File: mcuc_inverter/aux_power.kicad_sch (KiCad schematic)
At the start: 0 parts

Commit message: Capture aux_power sheet: full D020 rail tree, 7 blocks
INN3990CQ flyback per datasheet Fig. 10 / DER-948Q (series-string
input films, RCD clamp, custom 3-winding transformer symbol with
Lp/VOR/isolation notes, bias->BPP, Schottky secondary, FB 143k/13.2k
-> 14.97 V, SR and IS tied to GND per datasheet for diode operation);
LM5175 buck-boost aux path (15.02 V, deliberately above the
diode-dropped flyback so aux carries the load when present) through
LM74610-Q1 + external FET; two LMR51430 bucks (5 V: 71.5k/9.76k;
12 V: 115k/6.04k); TLV1117-33 3.3 V (PWR_FLAG moved here from the
MCU sheet - this is the rail's true source); 4x SN6505B + WE
750316856 gate supplies (winding CT pinout verified from the WE
drawing; +17.9/-5.1 zener splits); NXE2S0505MC isolated CAN 5 V.

All 12 VGD nets verified in the netlist to span aux_power sources
and gate_drive loads (e.g. VGD_HS1_P = rectifiers + caps + U301
VCC2), independently re-checked before commit. ERC 0 errors.

Co-Authored-By: Claude Fable 5 <noreply@anthropic.com>
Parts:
- added C601, C602: 0.68uF 630V film [TBV], Capacitor_SMD:C_0603_1608Metric, symbol Device:C
- added C603: 10nF 1kV [TBV], Capacitor_SMD:C_0603_1608Metric, symbol Device:C
- added C604: 10uF 50V [TBV], Capacitor_SMD:C_0603_1608Metric, symbol Device:C
- added C606: 4.7uF 25V X7R [TBV], Capacitor_SMD:C_0603_1608Metric, symbol Device:C
- added C607: 100nF [TBV], Capacitor_SMD:C_0603_1608Metric, symbol Device:C
- added C608: 1nF 100V [TBV], Capacitor_SMD:C_0603_1608Metric, symbol Device:C
- added C609, C610: 220uF 25V polymer [TBV], symbol Device:C_Polarized
- added C611, C622, C623, C642, C646, C661, C663, C665, C667, C669, C671, C673, C675, C677, C679, C681, C683: 100nF, Capacitor_SMD:C_0603_1608Metric, symbol Device:C
- added C612: 330pF [TBV], Capacitor_SMD:C_0603_1608Metric, symbol Device:C
- added C613, C625: 10nF [TBV], Capacitor_SMD:C_0603_1608Metric, symbol Device:C
- added C614: 2.2uF 25V X7R, Capacitor_SMD:C_0603_1608Metric, symbol Device:C
- added C620, C621: 4.7uF 50V [TBV], Capacitor_SMD:C_0805_2012Metric, symbol Device:C
- added C624: 4.7uF [TBV], Capacitor_SMD:C_0603_1608Metric, symbol Device:C
- added C626, C628: 100pF [TBV], Capacitor_SMD:C_0603_1608Metric, symbol Device:C
- added C627: 47nF [TBV], Capacitor_SMD:C_0603_1608Metric, symbol Device:C
- added C629, C630, C643, C644, C647, C648: 22uF 25V [TBV], Capacitor_SMD:C_1210_3225Metric, symbol Device:C
- added C631: 1uF [TBV], Capacitor_SMD:C_0603_1608Metric, symbol Device:C
- added C640, C645: 2.2uF 50V [TBV], Capacitor_SMD:C_0805_2012Metric, symbol Device:C
- added C650, C651, C653, C660, C666, C672, C678: 10uF [TBV], Capacitor_SMD:C_0805_2012Metric, symbol Device:C
- added C652: 2.2uF [TBV], Capacitor_SMD:C_0603_1608Metric, symbol Device:C
- added C662, C664, C668, C670, C674, C676, C680, C682: 10uF 25V [TBV], Capacitor_SMD:C_0805_2012Metric, symbol Device:C
- added D601: US1M-class 1kV std recovery [TBV], Diode_SMD:D_SOD-323, symbol Device:D
- added D602: BAS316-class [TBV], Diode_SMD:D_SOD-323, symbol Device:D
- added D603: SS310-class 100V 3A [TBV], Diode_SMD:D_SMA, symbol Device:D_Schottky
- added D604: SS54 [TBV], Diode_SMD:D_SMA, symbol Device:D_Schottky
- added D605, D606, D608, D609, D611, D612, D614, D615: SS310 [TBV], Diode_SMD:D_SMA, symbol Device:D_Schottky
- added D607, D610, D613, D616: BZX384-C5V1 [TBV], Diode_SMD:D_SOD-323, symbol Device:D_Zener
- added L601: 10uH [TBV], symbol Device:L
- added L602: 4.7uH [TBV], symbol Device:L
- added L603: 12uH [TBV], symbol Device:L
- added Q601, Q602, Q603, Q604, Q605: CSD18543Q3A-class [TBV], symbol Transistor_FET:CSD18543Q3A
- added R603, R604: 390k 0.5W [TBV], Resistor_SMD:R_0603_1608Metric, symbol Device:R
- added R605: 4.7R 0.5W [TBV], Resistor_SMD:R_0603_1608Metric, symbol Device:R
- added R606: 8.2k [TBV], Resistor_SMD:R_0603_1608Metric, symbol Device:R
- added R607: 100R [TBV], Resistor_SMD:R_0603_1608Metric, symbol Device:R
- added R608: 10R [TBV], Resistor_SMD:R_0603_1608Metric, symbol Device:R
- added R609: 143k 1%, Resistor_SMD:R_0603_1608Metric, symbol Device:R
- added R610: 13.2k 1%, Resistor_SMD:R_0603_1608Metric, symbol Device:R
- added R611: 10k [TBV], Resistor_SMD:R_0603_1608Metric, symbol Device:R
- added R620: 100k [TBV], Resistor_SMD:R_0603_1608Metric, symbol Device:R
- added R621: 16.2k [TBV], Resistor_SMD:R_0603_1608Metric, symbol Device:R
- added R622: 10mR 1% [TBV], Resistor_SMD:R_2512_6332Metric, symbol Device:R
- added R623: 88.7k 1%, Resistor_SMD:R_0603_1608Metric, symbol Device:R
- added R624: 4.99k 1%, Resistor_SMD:R_0603_1608Metric, symbol Device:R
- added R625: 24.9k [TBV], Resistor_SMD:R_0603_1608Metric, symbol Device:R
- added R626: 84.5k (300kHz) [TBV], Resistor_SMD:R_0603_1608Metric, symbol Device:R
- added R627: 93.1k (CCM+hiccup) [TBV], Resistor_SMD:R_0603_1608Metric, symbol Device:R
- added R640: 71.5k 1%, Resistor_SMD:R_0603_1608Metric, symbol Device:R
- added R641: 9.76k 1%, Resistor_SMD:R_0603_1608Metric, symbol Device:R
- added R642: 115k 1%, Resistor_SMD:R_0603_1608Metric, symbol Device:R
- added R643: 6.04k 1%, Resistor_SMD:R_0603_1608Metric, symbol Device:R
- added T601: custom flyback, Lp<500uH, VOR raised for 15 V out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, symbol mcuc:T_FLYBACK_AUX
- added T602, T603, T604, T605: 750316856, symbol mcuc:WE750316856
- added U601: INN3990CQ, symbol mcuc:INN3990CQ
- added U603: LM5175RHFR, symbol Regulator_Switching:LM5175RHF
- added U604: LM74610QDGKRQ1, symbol mcuc:LM74610-Q1
- added U605, U606: LMR51430XDDCR, symbol Regulator_Switching:LMR51430
- added U607: TLV1117-33, Package_TO_SOT_SMD:SOT-223-3_TabPin2, symbol Regulator_Linear:TLV1117-33
- added U608: NXE2S0505MC, symbol mcuc:NXE2S0505MC
- added U609, U610, U611, U612: SN6505BDBVR, symbol Power_Management:SN6505BDBV
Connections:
- new net: C642.2, L602.1, U605.2 (SW)
- new net: C642.1, U605.6 (CB)
- new net: D601.1 (K), R605.2
- new net: D601.2 (A), T601.2 (PRI-), U601.24 (D)
- new net: C612.1, C613.2, R609.2, R610.1, U601.3 (FB)
- new net: C603.2, R603.2, R604.2, R605.1
- new net: Q603.1 (G), U603.18 (LDRV2)
- new net: C614.1, U601.4 (BPS)
- new net: Q601.1 (G), U603.24 (HDRV1)
- new net: C613.1, R611.2
- new net: C606.1, C607.1, R606.2, U601.14 (BPP)
- new net: R607.2, U601.7 (FWD)
- new net: D606.2 (A), T602.4 (N4.B)
- new net: Q604.1 (G), U603.16 (HDRV2)
- new net: C623.1, U603.17 (BOOT2)
- new net: Q602.1 (G), U603.22 (LDRV1)
- new net: C622.1, U603.23 (BOOT1)
- new net: R620.2, R621.1, U603.26 (EN/UVLO)
- new net: D609.2 (A), T603.4 (N4.B)
- new net: D614.2 (A), T605.6 (N3.A)
- new net: D612.2 (A), T604.4 (N4.B)
- new net: D603.2 (A), R607.1, R608.1, T601.5 (SEC+)
- new net: C608.1, R608.2
- new net: C631.1, U604.7 (VCAPH)
- new net: C631.2, U604.1 (VCAPL)
- new net: D605.2 (A), T602.6 (N3.A)
- new net: C625.1, R625.2
- new net: T605.1 (N1.A), U612.1 (D1)
- new net: T605.3 (N2.B), U612.3 (D2)
- new net: C646.1, U606.6 (CB)
- new net: C646.2, L603.1, U606.2 (SW)
- new net: D615.2 (A), T605.4 (N4.B)
- new net: C601.2, C602.1
- new net: T603.1 (N1.A), U610.1 (D1)
- new net: T603.3 (N2.B), U610.3 (D2)
- new net: T602.1 (N1.A), U609.1 (D1)
- new net: T602.3 (N2.B), U609.3 (D2)
- new net: Q605.1 (G), U604.2 (GATE_PD), U604.6 (GATE_DRV)
- new net: C604.1, D602.1 (K), R606.1
- new net: D611.2 (A), T604.6 (N3.A)
- new net: D608.2 (A), T603.6 (N3.A)
- new net: D602.2 (A), T601.3 (BIAS+)
- new net: T604.1 (N1.A), U611.1 (D1)
- new net: T604.3 (N2.B), U611.3 (D2)
- new net +12V: C647.1, C648.1, L603.2, R642.1
- new net +3.3V: C651.1, U607.2 (VO)
- new net +5V: C643.1, C644.1, C650.1, C652.1, C660.1, C661.1, C666.1, C667.1, C672.1, C673.1, C678.1, C679.1, L602.2, R640.1, T602.2 (CT_PRI), T603.2 (CT_PRI), T604.2 (CT_PRI), T605.2 (CT_PRI), U607.3 (VI), U608.3 (+VIN), U609.2 (VCC), U609.5 (EN), U610.2 (VCC), U610.5 (EN), U611.2 (VCC), U611.5 (EN), U612.2 (VCC), U612.5 (EN)
- new net AUX_15V: C640.1, C645.1, D604.1 (K), Q605.3 (D), U604.8 (CATHODE), U605.3 (VIN), U605.5 (EN), U606.3 (VIN), U606.5 (EN)
- new net AUX_IN: C620.1, C621.1, Q601.3 (D), R620.1, U603.27 (VIN), U603.28 (VISNS)
- new net BB_15V: C629.1, C630.1, Q604.3 (D), Q605.2 (S), R623.1, U603.10 (ISNS(-)), U603.11 (ISNS(+)), U603.21 (BIAS), U603.9 (VOSNS), U604.4 (ANODE)
- new net BB_COMP: C626.1, R625.1, U603.6 (COMP)
- new net BB_CS: Q602.2 (S), Q603.2 (S), R622.1, U603.13 (CS)
- new net BB_FB: R623.2, R624.1, U603.8 (FB)
- new net BB_MODE: R627.1, U603.1 (MODE)
- new net BB_RT: R626.1, U603.3 (RT/SYNC)
- new net BB_SLOPE: C628.1, U603.4 (SLOPE)
- new net BB_SS: C627.1, U603.5 (SS)
- new net BB_SW1: C622.2, L601.1, Q601.2 (S), Q602.3 (D), U603.25 (SW1)
- new net BB_SW2: C623.2, L601.2, Q603.3 (D), Q604.2 (S), U603.15 (SW2)
- new net BB_VCC: C624.1, U603.20 (VCC)
- new net CAN_5V: C653.1, U608.8 (+VOUT)
- new net CAN_GND: C653.2, U608.7 (-VOUT)
- new net DC_BUS_N: C602.2, C604.2, C606.2, C607.2, T601.4 (BIAS-), U601.13 (V), U601.16 (S), U601.17 (S), U601.18 (S), U601.19 (S)
- new net DC_BUS_P: C601.1, C603.1, R603.1, R604.1, T601.1 (PRI+)
- new net FB_12V: R642.2, R643.1, U606.4 (FB)
- new net FB_5V: R640.2, R641.1, U605.4 (FB)
- new net FLY_15V: C608.2, C609.1, C610.1, C611.1, D603.1 (K), D604.2 (A), R609.1, R611.1, U601.6 (VOUT)
- new net GND: C609.2, C610.2, C611.2, C612.2, C614.2, C620.2, C621.2, C624.2, C625.2, C626.2, C627.2, C628.2, C629.2, C630.2, C640.2, C643.2, C644.2, C645.2, C647.2, C648.2, C650.2, C651.2, C652.2, C660.2, C661.2, C666.2, C667.2, C672.2, C673.2, C678.2, C679.2, R610.2, R621.2, R622.2, R624.2, R626.2, R627.2, R641.2, R643.2, T601.6 (SEC-), U601.1 (IS), U601.2 (GND), U601.5 (SR), U603.12 (CSG), U603.19 (PGND), U603.2 (DITH), U603.29 (PowerPAD), U603.7 (AGND), U605.1 (GND), U606.1 (GND), U607.1 (GND), U608.1 (-VIN), U609.4 (GND), U609.6 (CLK), U610.4 (GND), U610.6 (CLK), U611.4 (GND), U611.6 (CLK), U612.4 (GND), U612.6 (CLK)
- new net VGD_HS1_COM: C662.2, C663.2, C664.1, C665.1, D607.1 (K)
- new net VGD_HS1_N: C664.2, C665.2, D607.2 (A), T602.5 (CT_SEC)
- new net VGD_HS1_P: C662.1, C663.1, D605.1 (K), D606.1 (K)
- new net VGD_HS2_COM: C668.2, C669.2, C670.1, C671.1, D610.1 (K)
- new net VGD_HS2_N: C670.2, C671.2, D610.2 (A), T603.5 (CT_SEC)
- new net VGD_HS2_P: C668.1, C669.1, D608.1 (K), D609.1 (K)
- new net VGD_HS3_COM: C674.2, C675.2, C676.1, C677.1, D613.1 (K)
- new net VGD_HS3_N: C676.2, C677.2, D613.2 (A), T604.5 (CT_SEC)
- new net VGD_HS3_P: C674.1, C675.1, D611.1 (K), D612.1 (K)
- new net VGD_LS_COM: C680.2, C681.2, C682.1, C683.1, D616.1 (K)
- new net VGD_LS_N: C682.2, C683.2, D616.2 (A), T605.5 (CT_SEC)
- new net VGD_LS_P: C680.1, C681.1, D614.1 (K), D615.1 (K)
- no-connect marks 0 -> 3
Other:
- note added: "+17.9 V"
- note added: "+5V / +12V / +3.3V / GND are global power rails sourced on this sheet (PWR_FLAG on +5V here; +12V flagged on precharge sheet, +3.3V and GND flagged on MCU sheet - no duplicates)."
- note added: "-5.1 V"
- note added: "AUX input: LM5175 4-switch buck-boost, 12-24 V in -> 15.02 V (FB 88.7k/4.99k @ 0.8 V). fsw 300 kHz (RT 84.5k), CCM+hiccup (MODE 93.1k), all loop/support values [TBV]. EN divider 100k/16.2k -> input UVLO ~8.9 V [TBV]. ISNS+/- shorted (CC loop disabled)."
- note added: "CAN supply: functional 3 kVDC isolation. CAN_GND is the isolated CAN return - do not tie to GND."
- note added: "D604 SS54: plain Schottky OR from flyback into AUX_15V. Penalty ~0.4 V / ~0.7 W at 1.7 A. Upgrade: second LM74610+FET stage [TBV]. Flyback is the primary source; the LM5175 aux path carries the board only when the 12-24 V feed is present (15.02 V > 14.97 - 0.4 V)."
- note added: "Gate-drive supplies (x4): SN6505B push-pull from +5V (SN6505B is 5 V-only, D020) + WE 750316856 (1:4.67 CT:CT) -> ~23 V raw full-wave rail. BZX384-C5V1 zener from raw(-) sets COM 5.1 V above it: P-COM = +17.9 V, COM-N = -5.1 V. Transformer isolation is functional (2.5 kVac); the reinforced barrier remains in the 1ED3491 drivers (SPEC 5, D017). Net names match gate_drive sheet pins."
- note added: "ISOLATION: primary side of T601 floats at HV bus potential (48-450 V, 500 V transient). Spacing per SPEC 10: >=3.2 mm clearance / >=6.4 mm creepage power->control, T601 reinforced >=4 kV. FluxLink feedback is internal to U601 (no optocoupler). Film caps C601/C602 in series so no single part spans the full bus (SPEC 8.2). Optional CM choke placeholder: fit 2x wire links / CMC [TBV] in the DC_BUS_P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"
- note added: "Primary OVP chain (not fitted - note per datasheet): zener + series R + blocking diode from the rectified bias rail into BPP triggers latching OVP at ISD. Fit if secondary OVP insufficient [TBV]."
- note added: "SPEC.md 11.2b - DECISIONS.md D020. HV flyback (INN3990CQ) -> 15 V main rail; LM5175 buck-boost from 12-24 V AUX_IN OR'd in via LM74610 smart diode; LMR51430 bucks -> 5 V / 12 V; TLV1117 -> 3.3 V; 4x SN6505B+750316856 gate supplies; NXE2S0505MC CAN 5 V."
- note added: "SR pin tied to GND: diode-only rectification (datasheet: 'If no SR FET is used connect this pin to GND'). IS tied to GND: no CC regulation. FB divider 143k/13.2k @ 1.265 V ref -> 14.97 V. Feed-forward 10k + 10 nF per Fig 10."
- note added: "V pin tied to SOURCE: line UV/OV sense not used (48-450 V range guaranteed by design). Optional 4x series 390k sense chain per AN-106 [TBV]."
- note removed: "Placeholder. Requirements: SPEC.md 11"

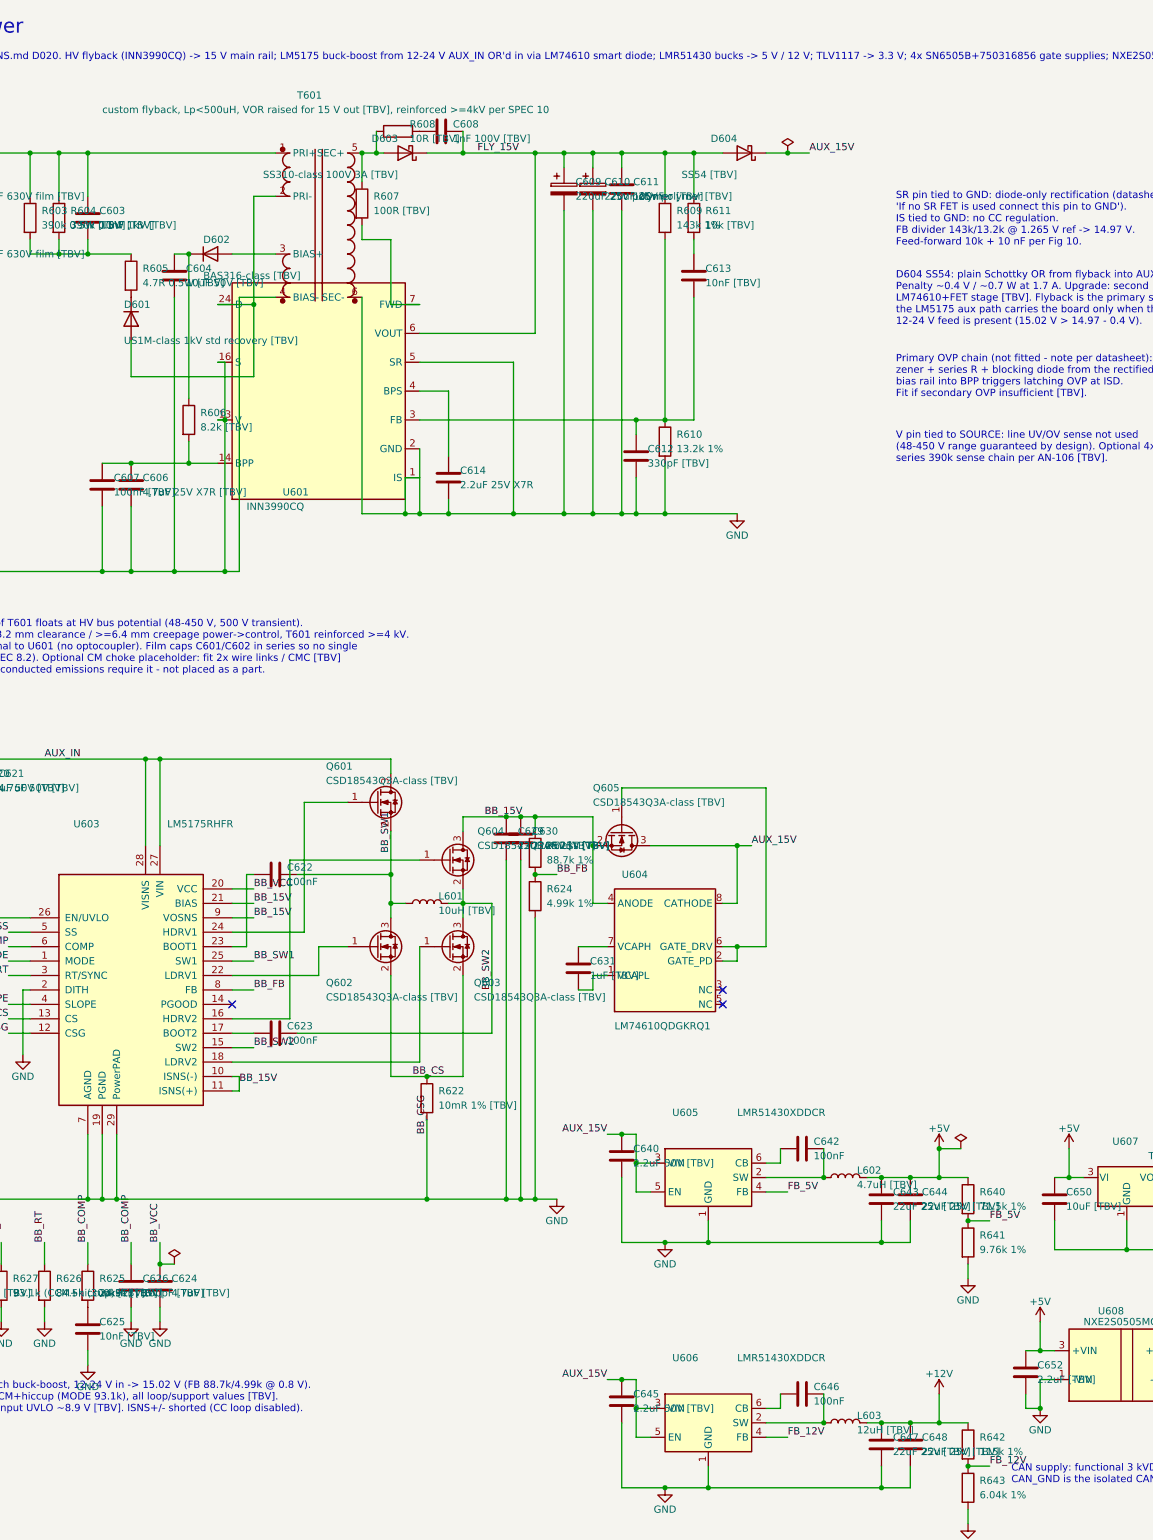
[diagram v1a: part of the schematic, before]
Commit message: Board-prep: footprint audit complete, HV terminals, off-board flags
474-component audit: 466 valid resolved footprints, 13 off-board
exclusions per D024 (caps to carrier, chassis resistors, HOYS), 4
flagged TBDs (custom flyback + 3 unchosen inductors), zero silent
gaps. Netlist-fatal fixes: Q403 renumbered to Wolfspeed TO-263-7
convention (G1/KS2/S3-7/tab-D8), CSD18543Q3A remapped to KiCad's
SSSGD VSON-8 pairing - both verified in the netlist afterward.

New HV interface terminals J401-J405 (M4 ring-lug pads: DC input,
precharge-R chassis loop, discharge-R return, bus taps) and HOYS
harness headers J501-J503 (JST 2mm; PA-vs-PH footprint flagged TBV)
with net membership machine-verified incl. the OC_TRIP wire-OR and
I_REF paths to the MCU ADCs.

ERC 0 errors, warnings 201 -> 200 (none introduced).

Co-Authored-By: Claude Fable 5 <noreply@anthropic.com>
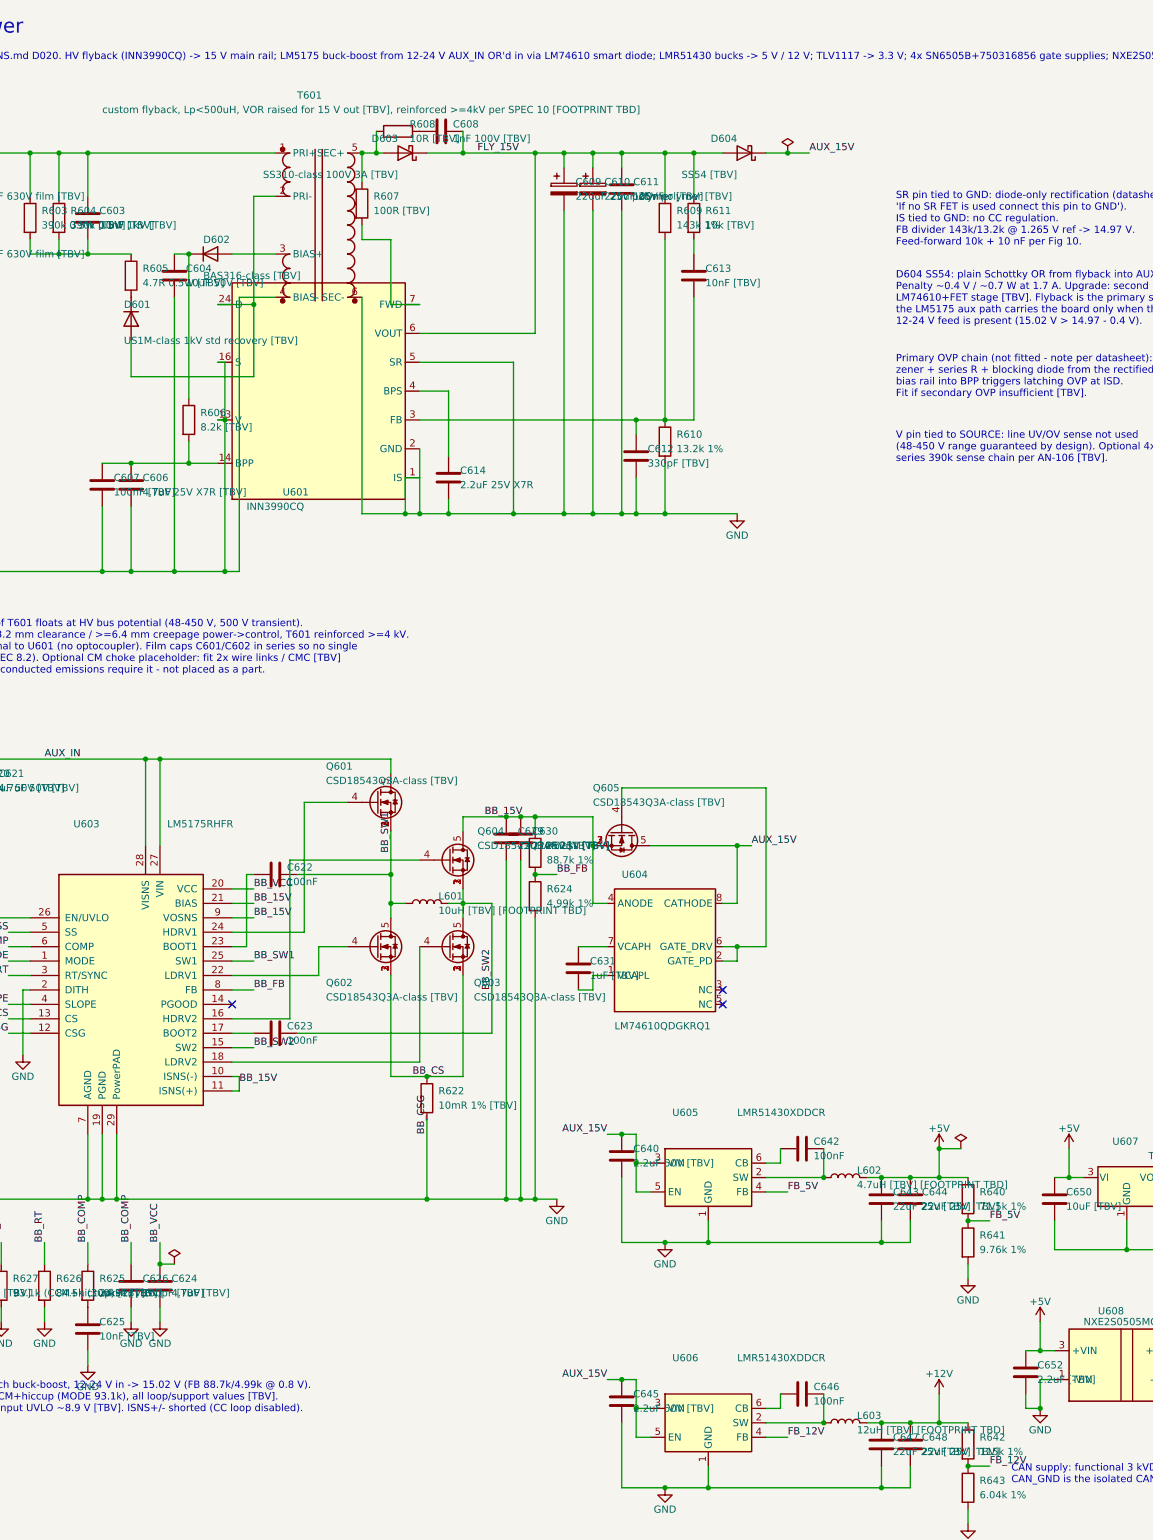
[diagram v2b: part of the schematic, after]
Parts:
- C609, C610: footprint (none) -> Capacitor_SMD:CP_Elec_8x10.5
- D601: footprint Diode_SMD:D_SOD-323 -> Diode_SMD:D_SMA
- D603, D604, D605, D606, D608, D609, D611, D612, D614, D615: footprint Diode_SMD:D_SMA -> Diode_SMD:D_SMC
- L601: value 10uH [TBV] -> 10uH [TBV] [FOOTPRINT TBD]
- L602: value 4.7uH [TBV] -> 4.7uH [TBV] [FOOTPRINT TBD]
- L603: value 12uH [TBV] -> 12uH [TBV] [FOOTPRINT TBD]
- Q601, Q602, Q603, Q604, Q605: footprint (none) -> Package_SON:VSON-8_3.3x3.3mm_P0.65mm_NexFET
- T601: value custom flyback, Lp<500uH, VOR raised for 15 V out [TBV], reinforced >=4kV per SPEC 10 -> custom flyback, Lp<500uH, VOR raised for 15 V out [TBV], reinforced >=4kV per SPEC 10 [FOOTPRINT TBD]
- T602, T603, T604, T605: footprint (none) -> mcuc:WE_PPTI_750316856
- U601: footprint (none) -> mcuc:InSOP-24D
- U603: footprint (none) -> Package_DFN_QFN:VQFN-28-1EP_4x5mm_P0.5mm_EP2.55x3.55mm
- U604: footprint (none) -> Package_SO:VSSOP-8_3x3mm_P0.65mm
- U605, U606, U609, U610, U611, U612: footprint (none) -> Package_TO_SOT_SMD:SOT-23-6
- U608: footprint (none) -> Converter_DCDC:Converter_DCDC_Murata_NXExSxxxxMC_SMD
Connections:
- net AUX_15V: now also Q605.5 (D); no longer Q605.3 (D)
- net AUX_IN: now also Q601.5 (D); no longer Q601.3 (D)
- net BB_15V: now also Q604.5 (D), Q605.1 (S), Q605.3 (S); no longer Q604.3 (D)
- net BB_CS: now also Q602.1 (S), Q602.3 (S), Q603.1 (S), Q603.3 (S)
- net BB_SW1: now also Q601.1 (S), Q601.3 (S), Q602.5 (D); no longer Q602.3 (D)
- net BB_SW2: now also Q603.5 (D), Q604.1 (S), Q604.3 (S); no longer Q603.3 (D)
- net at U603.18 (LDRV2): now also Q603.4 (G); no longer Q603.1 (G)
- net at U603.24 (HDRV1): now also Q601.4 (G); no longer Q601.1 (G)
- net at U603.16 (HDRV2): now also Q604.4 (G); no longer Q604.1 (G)
- net at U603.22 (LDRV1): now also Q602.4 (G); no longer Q602.1 (G)
- net at U604.2 (GATE_PD), U604.6 (GATE_DRV): now also Q605.4 (G); no longer Q605.1 (G)
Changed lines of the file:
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@@
 			)
 		)
-		(property "Footprint" "Diode_SMD:D_SOD-323"
+		(property "Footprint" "Diode_SMD:D_SMA"
 			(at 66.04 69.85 0)
 			(effects
@@
 			)
 		)
-		(property "Value" "custom flyback, Lp<500uH, VOR raised for 15 V out [TBV], reinforced >=4kV per SPEC 10"
+		(property "Value" "custom flyback, Lp<500uH, VOR raised for 15 V out [TBV], reinforced >=4kV per SPEC 10 [FOOTPRINT TBD]"
 			(at 60.96 33.02 0)
 			(effects
@@
 			)
 		)
-		(property "Footprint" ""
+		(property "Footprint" "mcuc:InSOP-24D"
 			(at 99.06 82.55 0)
 			(effects
@@
 			)
 		)
-		(property "Footprint" "Diode_SMD:D_SMA"
+		(property "Footprint" "Diode_SMD:D_SMC"
 			(at 114.3 40.64 0)
 			(effects
@@
 			)
 		)
-		(property "Footprint" ""
+		(property "Footprint" "Capacitor_SMD:CP_Elec_8x10.5"
 			(at 142.24 46.99 0)
 			(effects
@@
 			)
 		)
-		(property "Footprint" ""
+		(property "Footprint" "Capacitor_SMD:CP_Elec_8x10.5"
 			(at 147.32 46.99 0)
 			(effects
@@
 			)
 		)
-		(property "Footprint" "Diode_SMD:D_SMA"
+		(property "Footprint" "Diode_SMD:D_SMC"
 			(at 173.99 40.64 0)
 			(effects
@@
 			)
 		)
-		(property "Footprint" ""
+		(property "Footprint" "Package_DFN_QFN:VQFN-28-1EP_4x5mm_P0.5mm_EP2.55x3.55mm"
 			(at 66.04 187.96 0)
 			(effects
@@
 			)
 		)
-		(property "Footprint" ""
+		(property "Footprint" "Package_SON:VSON-8_3.3x3.3mm_P0.65mm_NexFET"
 			(at 109.22 154.94 0)
 			(effects
@@
 			)
 		)
-		(property "Footprint" ""
+		(property "Footprint" "Package_SON:VSON-8_3.3x3.3mm_P0.65mm_NexFET"
 			(at 109.22 180.34 0)
 			(effects
@@
 			)
 		)
-		(property "Footprint" ""
+		(property "Footprint" "Package_SON:VSON-8_3.3x3.3mm_P0.65mm_NexFET"
 			(at 121.92 180.34 0)
 			(effects
@@
 			)
 		)
-		(property "Footprint" ""
+		(property "Footprint" "Package_SON:VSON-8_3.3x3.3mm_P0.65mm_NexFET"
 			(at 121.92 165.1 0)
 			(effects
@@
 			)
 		)
-		(property "Value" "10uH [TBV]"
+		(property "Value" "10uH [TBV] [FOOTPRINT TBD]"
 			(at 120.142 173.99 270)
 			(effects
@@
 			)
 		)
-		(property "Footprint" ""
+		(property "Footprint" "Package_SON:VSON-8_3.3x3.3mm_P0.65mm_NexFET"
 			(at 152.4 160.02 0)
 			(effects
@@
 			)
 		)
-		(property "Footprint" ""
+		(property "Footprint" "Package_SO:VSSOP-8_3x3mm_P0.65mm"
 			(at 160.02 180.34 0)
 			(effects
@@
 			)
 		)
-		(property "Footprint" ""
+		(property "Footprint" "Package_TO_SOT_SMD:SOT-23-6"
 			(at 167.64 220.98 0)
 			(effects
@@
 			)
 		)
-		(property "Value" "4.7uH [TBV]"
+		(property "Value" "4.7uH [TBV] [FOOTPRINT TBD]"
 			(at 193.80200000000002 222.25 270)
 			(effects
@@
 			)
 		)
-		(property "Footprint" ""
+		(property "Footprint" "Package_TO_SOT_SMD:SOT-23-6"
 			(at 167.64 264.16 0)
 			(effects
@@
 			)
 		)
-		(property "Value" "12uH [TBV]"
+		(property "Value" "12uH [TBV] [FOOTPRINT TBD]"
 			(at 193.80200000000002 265.43 270)
 			(effects
@@
 			)
 		)
-		(property "Footprint" ""
+		(property "Footprint" "Converter_DCDC:Converter_DCDC_Murata_NXExSxxxxMC_SMD"
 			(at 241.3 254.0 0)
 			(effects
@@
 			)
 		)
-		(property "Footprint" ""
+		(property "Footprint" "Package_TO_SOT_SMD:SOT-23-6"
 			(at 294.64 58.42 0)
 			(effects
@@
 			)
 		)
-		(property "Footprint" ""
+		(property "Footprint" "mcuc:WE_PPTI_750316856"
 			(at 317.5 55.88 0)
 			(effects
@@
 			)
 		)
-		(property "Footprint" "Diode_SMD:D_SMA"
+		(property "Footprint" "Diode_SMD:D_SMC"
 			(at 334.01 45.72 0)
 			(effects
@@
 			)
 		)
-		(property "Footprint" "Diode_SMD:D_SMA"
+		(property "Footprint" "Diode_SMD:D_SMC"
 			(at 334.01 66.04 0)
 			(effects
@@
 			)
 		)
-		(property "Footprint" ""
+		(property "Footprint" "Package_TO_SOT_SMD:SOT-23-6"
 			(at 294.64 116.84 0)
 			(effects
@@
 			)
 		)
-		(property "Footprint" ""
+		(property "Footprint" "mcuc:WE_PPTI_750316856"
 			(at 317.5 114.3 0)
 			(effects
@@
 			)
 		)
-		(property "Footprint" "Diode_SMD:D_SMA"
+		(property "Footprint" "Diode_SMD:D_SMC"
 			(at 334.01 104.14 0)
 			(effects
@@
 			)
 		)
-		(property "Footprint" "Diode_SMD:D_SMA"
+		(property "Footprint" "Diode_SMD:D_SMC"
 			(at 334.01 124.46 0)
 			(effects
@@
 			)
 		)
-		(property "Footprint" ""
+		(property "Footprint" "Package_TO_SOT_SMD:SOT-23-6"
 			(at 294.64 175.26 0)
 			(effects
@@
 			)
 		)
-		(property "Footprint" ""
+		(property "Footprint" "mcuc:WE_PPTI_750316856"
 			(at 317.5 172.72 0)
 			(effects
@@
 			)
 		)
-		(property "Footprint" "Diode_SMD:D_SMA"
+		(property "Footprint" "Diode_SMD:D_SMC"
 			(at 334.01 162.56 0)
 			(effects
@@
 			)
 		)
-		(property "Footprint" "Diode_SMD:D_SMA"
+		(property "Footprint" "Diode_SMD:D_SMC"
 			(at 334.01 182.88 0)
 			(effects
@@
 			)
 		)
-		(property "Footprint" ""
+		(property "Footprint" "Package_TO_SOT_SMD:SOT-23-6"
 			(at 294.64 233.68 0)
 			(effects
@@
 			)
 		)
-		(property "Footprint" ""
+		(property "Footprint" "mcuc:WE_PPTI_750316856"
 			(at 317.5 231.14000000000001 0)
 			(effects
@@
 			)
 		)
-		(property "Footprint" "Diode_SMD:D_SMA"
+		(property "Footprint" "Diode_SMD:D_SMC"
 			(at 334.01 220.98000000000002 0)
 			(effects
@@
 			)
 		)
-		(property "Footprint" "Diode_SMD:D_SMA"
+		(property "Footprint" "Diode_SMD:D_SMC"
 			(at 334.01 241.3 0)
 			(effects
